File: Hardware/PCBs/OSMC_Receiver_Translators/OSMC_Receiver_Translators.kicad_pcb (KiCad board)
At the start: 4 copper layers, 120.1 x 78.2 mm, 83 parts, among them J1 Conn_01x04, J10 Conn_01x04, J11 Conn_01x04, J12 Conn_01x04, J13 Conn_01x04, J14 Conn_01x04, J15 Conn_01x04, J16 Conn_01x04, J2 Conn_01x04, J3 Conn_01x04, J4 Conn_01x04, J5 Conn_01x04, J6 Conn_01x04, J7 Conn_01x04, J8 Conn_01x04, J9 Conn_01x04, U1 24AA02-OT, U13 OSMC Module Board, U14 OSMC Module Board, U15 OSMC Module Board, U16 OSMC Module Board, U17 OSMC Module Board, U18 OSMC Module Board, U19 OSMC Module Board, U2 LTC4317, U20 OSMC Module Board, U3 XIAO-ESP32-S3-DIP, U4 PCF8574DWR, U5 LTC4317, U6 LTC4317, U7 LTC4317

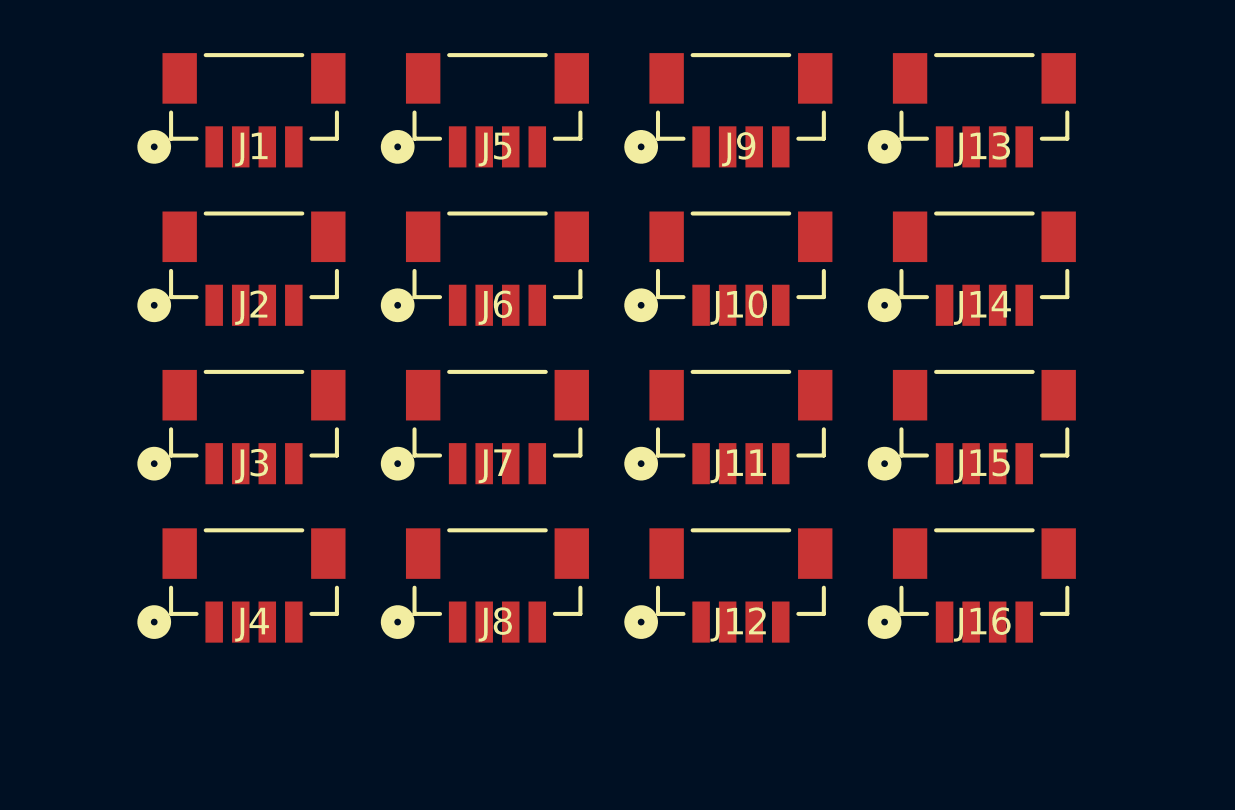
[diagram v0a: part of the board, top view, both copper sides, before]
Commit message: remove connectors
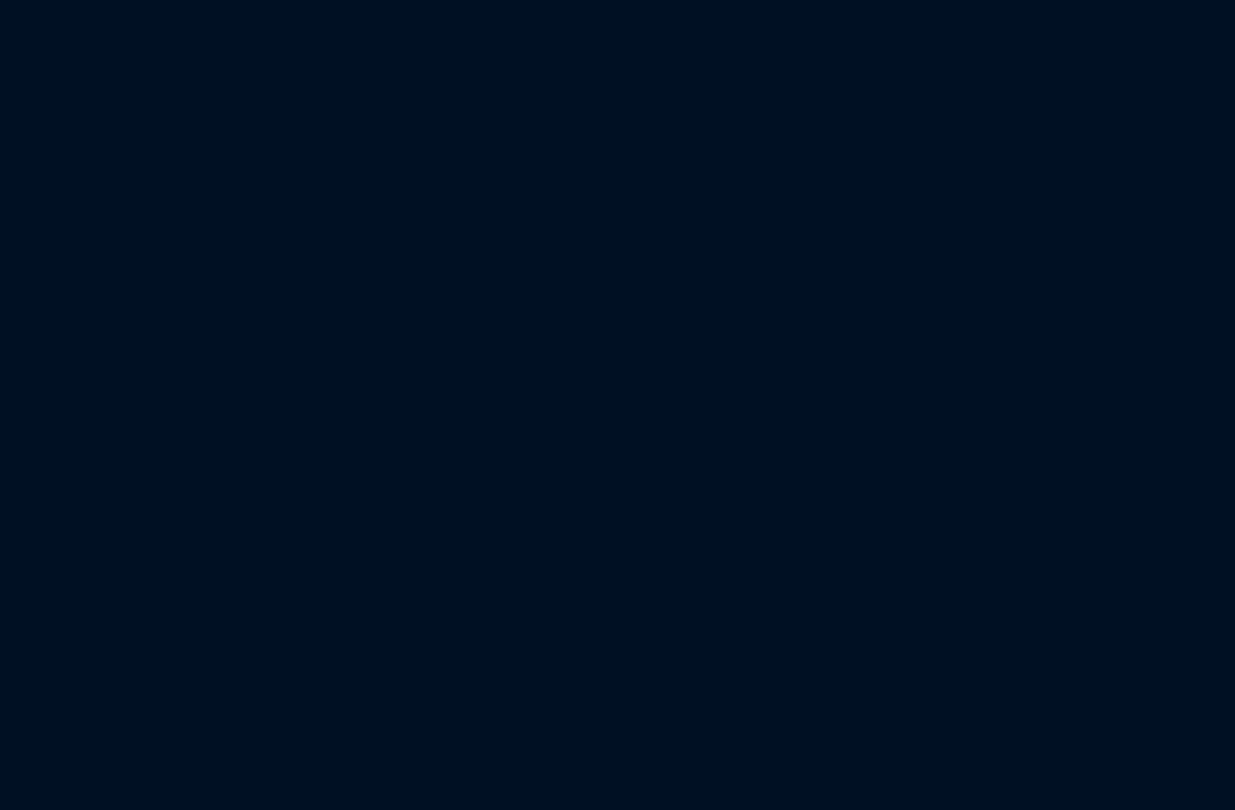
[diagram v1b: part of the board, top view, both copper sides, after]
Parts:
- removed J1, J10, J11, J12, J13, J14, J15, J16, J2, J3, J4, J5, J6, J7, J8, J9: Conn_01x04, OSMC_Module:CONN4_BM04B-SRSS_JST
